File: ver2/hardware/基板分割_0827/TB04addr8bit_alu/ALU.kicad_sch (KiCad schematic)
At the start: 8 parts, among them J801 Conn_02x05_Odd_Even, J802 Conn_02x05_Odd_Even, J803 Conn_02x05_Odd_Even, J804 Conn_02x05_Odd_Even, J805 Conn_02x05_Odd_Even, J806 Conn_02x05_Odd_Even, J807 Conn_02x05_Odd_Even, J808 Conn_02x05_Odd_Even

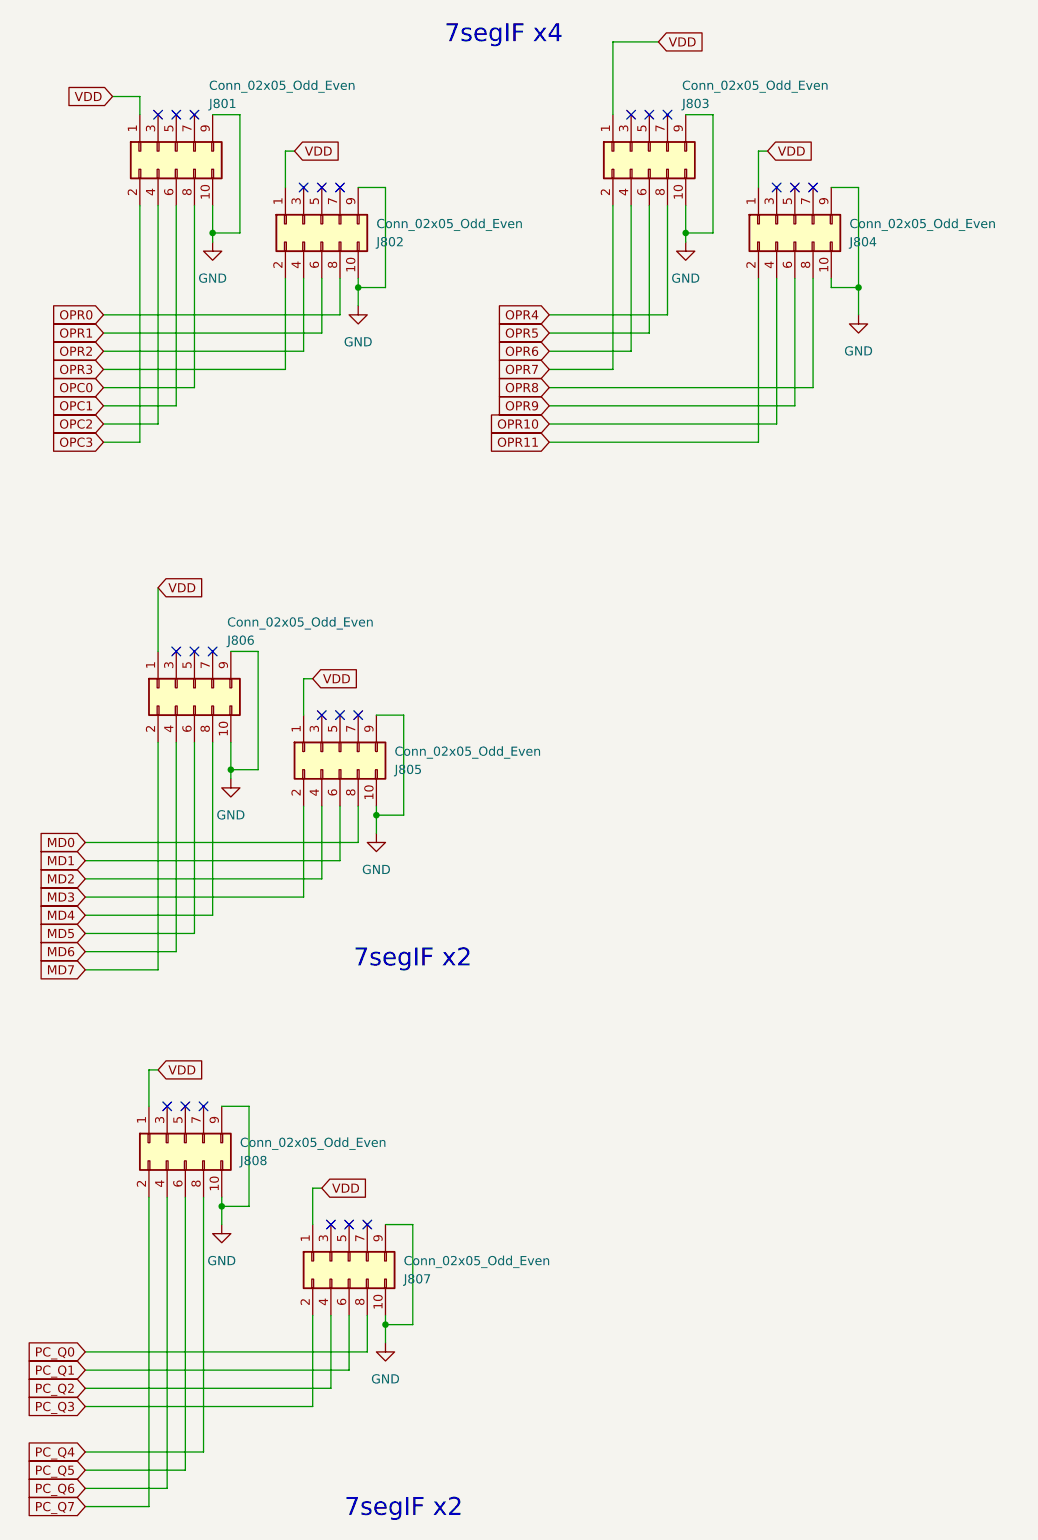
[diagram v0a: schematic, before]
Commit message: ver2: 3分割でシート内の不要部品・配線を削除(検証合格)／キャリアを0827へコピー
- 制御34・演算25・IF10=IC69でマスターと一致、部品の取りこぼし0
- ピン-ネット署名の変化0件=誤って線を切った箇所なし
- またぐ信号は制御/演算35・IF/制御18で手順書の表と過不足ゼロ

Co-Authored-By: Claude Opus 5 <noreply@anthropic.com>
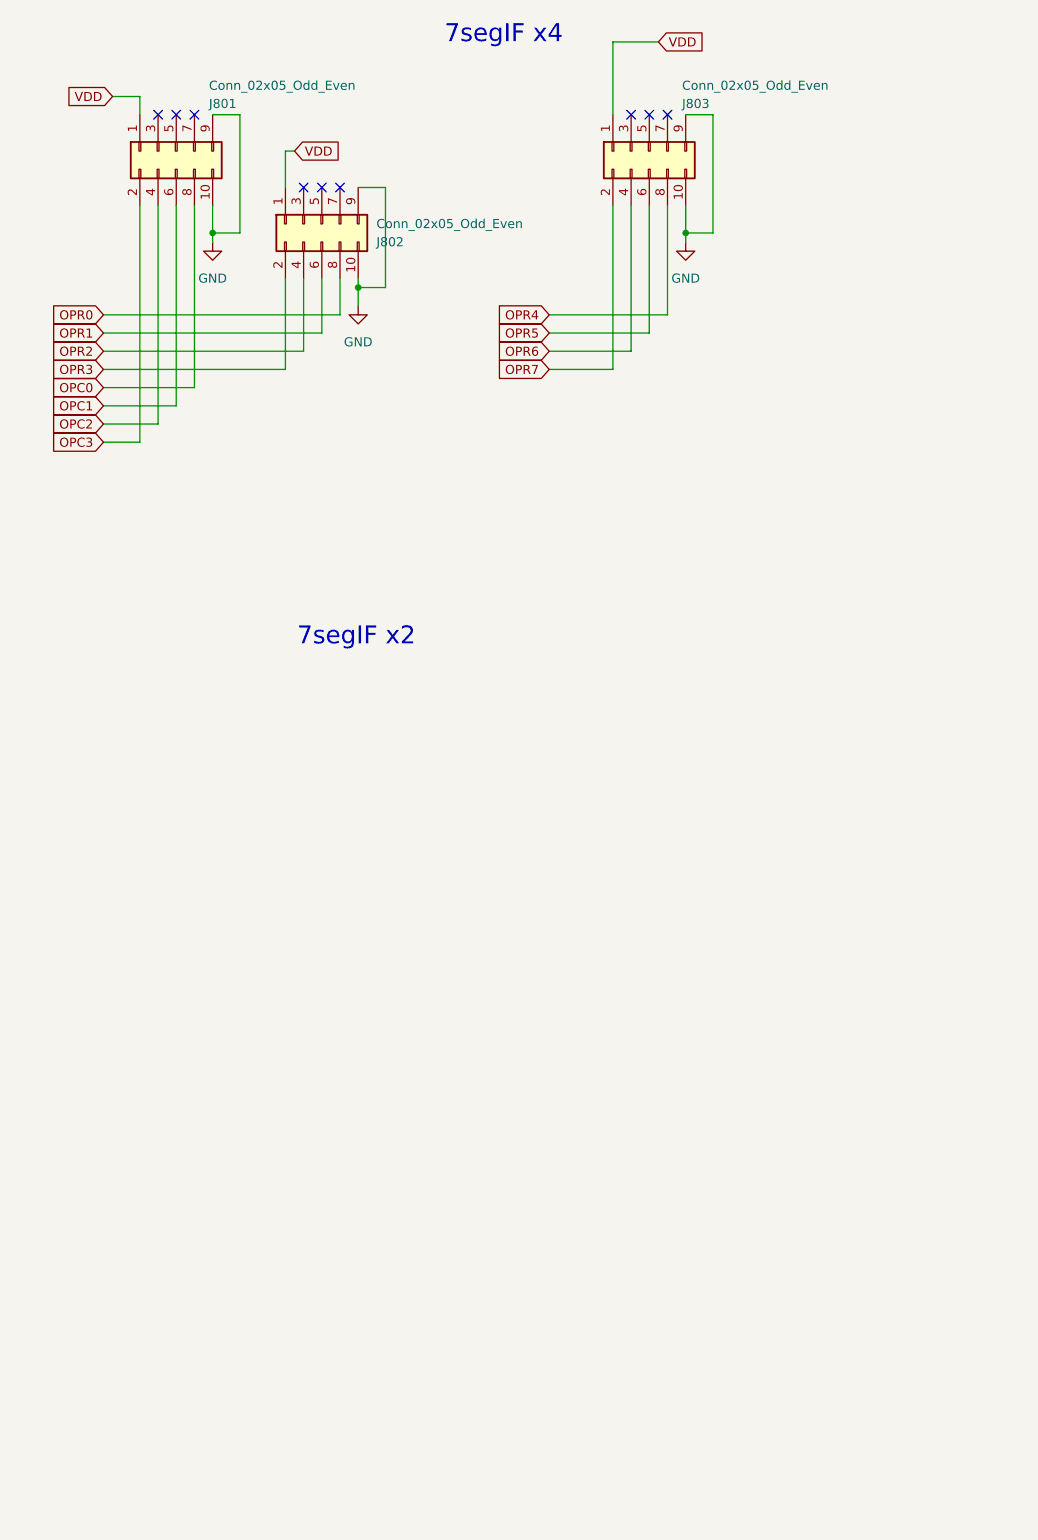
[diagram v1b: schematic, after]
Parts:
- removed J804, J805, J806, J807, J808: Conn_02x05_Odd_Even, Connector_PinSocket_2.54mm:PinSocket_2x05_P2.54mm_Vertical, symbol Connector_Generic:Conn_02x05_Odd_Even
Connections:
- no-connect marks 24 -> 9

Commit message: ver2: 演算板にInterFaceシートを復元(_copyからコピー・J801-808)
- 命令表示(OPC/OPR)を演算板へ集約する方針変更に伴う復元
- 旧プロジェクト名16箇所を_aluへ置換、パース確認済み(部品99→104)

Co-Authored-By: Claude Opus 5 <noreply@anthropic.com>
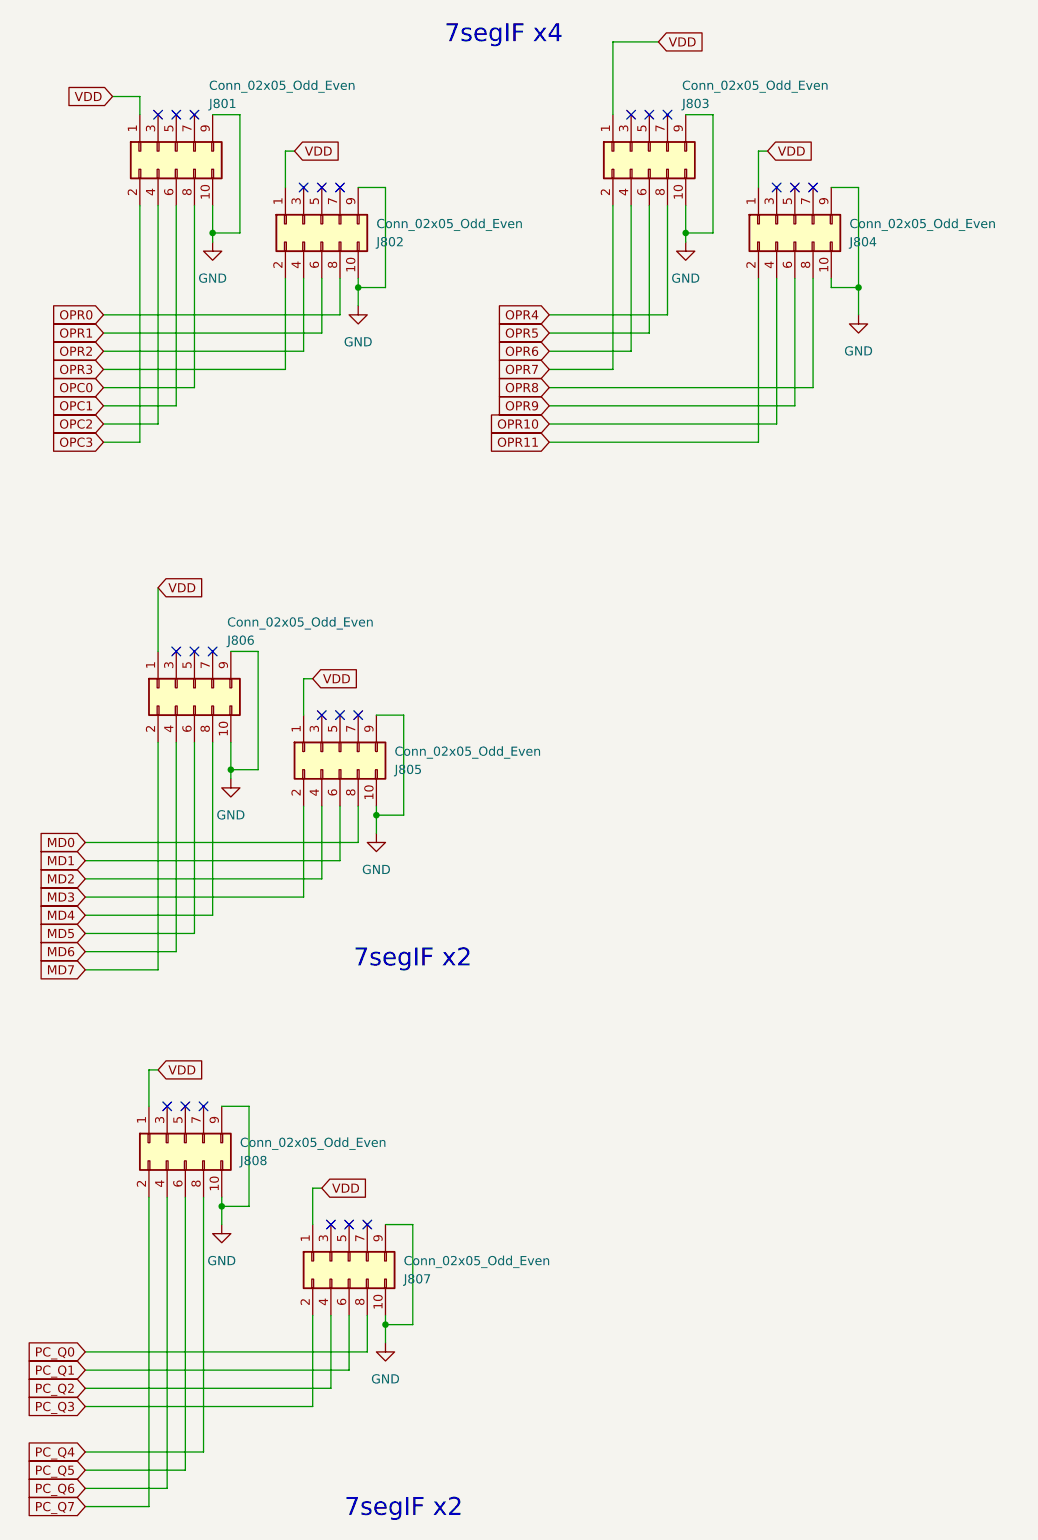
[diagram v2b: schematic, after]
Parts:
- added J804, J805, J806, J807, J808: Conn_02x05_Odd_Even, Connector_PinSocket_2.54mm:PinSocket_2x05_P2.54mm_Vertical, symbol Connector_Generic:Conn_02x05_Odd_Even
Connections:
- net GND: now also J804.10 (Pin_10), J804.9 (Pin_9), J805.10 (Pin_10), J805.9 (Pin_9), J806.10 (Pin_10), J806.9 (Pin_9), J807.10 (Pin_10), J807.9 (Pin_9), J808.10 (Pin_10), J808.9 (Pin_9)
- net VDD: now also J804.1 (Pin_1), J805.1 (Pin_1), J806.1 (Pin_1), J807.1 (Pin_1), J808.1 (Pin_1)
- new net MD0: J805.8 (Pin_8)
- new net MD1: J805.6 (Pin_6)
- new net MD2: J805.4 (Pin_4)
- new net MD3: J805.2 (Pin_2)
- new net MD4: J806.8 (Pin_8)
- new net MD5: J806.6 (Pin_6)
- new net MD6: J806.4 (Pin_4)
- new net MD7: J806.2 (Pin_2)
- new net OPR10: J804.4 (Pin_4)
- new net OPR11: J804.2 (Pin_2)
- new net OPR8: J804.8 (Pin_8)
- new net OPR9: J804.6 (Pin_6)
- new net PC_Q0: J807.8 (Pin_8)
- new net PC_Q1: J807.6 (Pin_6)
- new net PC_Q2: J807.4 (Pin_4)
- new net PC_Q3: J807.2 (Pin_2)
- new net PC_Q4: J808.8 (Pin_8)
- new net PC_Q5: J808.6 (Pin_6)
- new net PC_Q6: J808.4 (Pin_4)
- new net PC_Q7: J808.2 (Pin_2)
- no-connect marks 9 -> 24
